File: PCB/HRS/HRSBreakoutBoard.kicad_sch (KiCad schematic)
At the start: 14 parts, among them J1 Conn_01x15, U2 AD7476A, U3 epc901

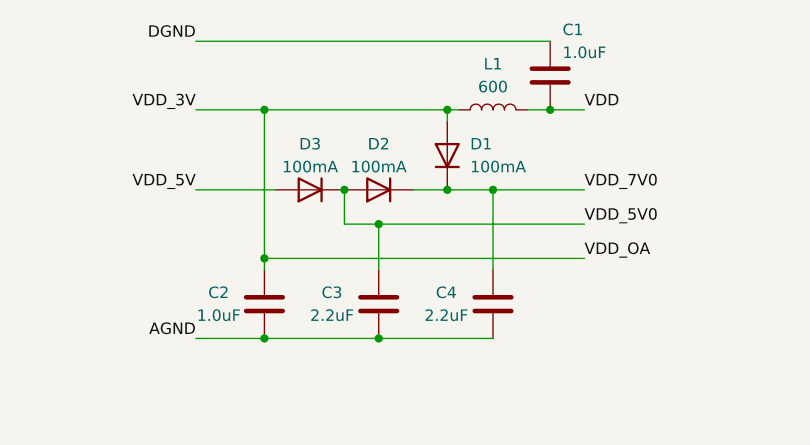
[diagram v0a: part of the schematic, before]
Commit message: Completed footprints and schematics
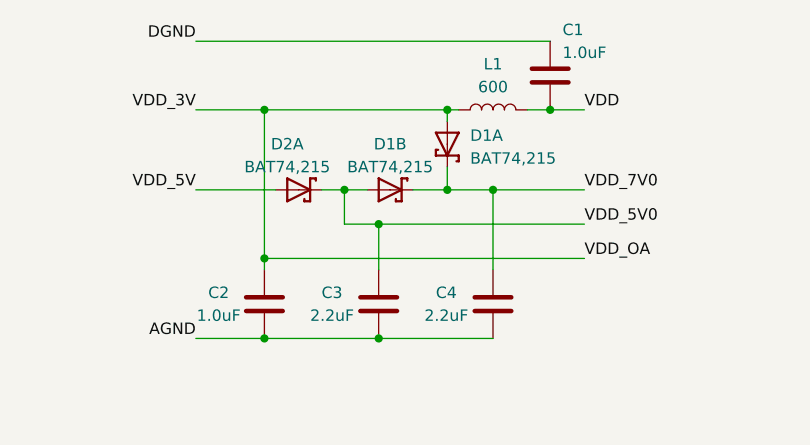
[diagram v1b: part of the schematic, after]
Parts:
- removed D1, D2, D3: 100mA, symbol Device:D
- added D1, D2: BAT74,215, HRS:SOT143(B), symbol HRS:BAT74,215
- C1, C2, C3, C4, C5, C6: footprint (none) -> HRS:C_0603_1608Metric
- J1: footprint (none) -> HRS:Breakout Board Connector
- L1: footprint (none) -> HRS:BEADC1005X55N
- R3: footprint (none) -> HRS:R_0603_1608Metric
- U2: footprint (none) -> HRS:AD7476
- U3: footprint (none) -> HRS:EPC901
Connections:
- net VDD_3V: now also D1.4
- net VDD_5V: now also D2.4
- net VDD_5V0: now also D1.3, D2.1
- net VDD_7V0: now also D1.1, D1.2
